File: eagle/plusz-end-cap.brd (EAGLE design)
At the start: 106 x 106 mm, 28 parts, among them U1 TCA9543A-PW, U3 HMC5883L, U4 HMC5883L

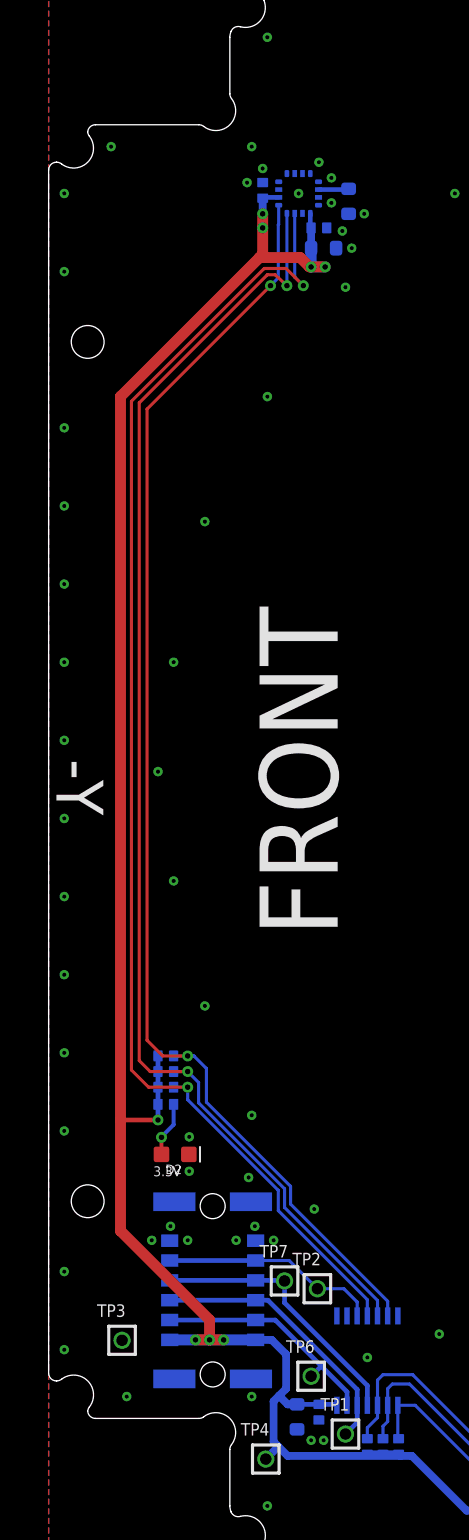
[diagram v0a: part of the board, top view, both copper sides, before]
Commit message: Added cutout for debug connector, update PNG.
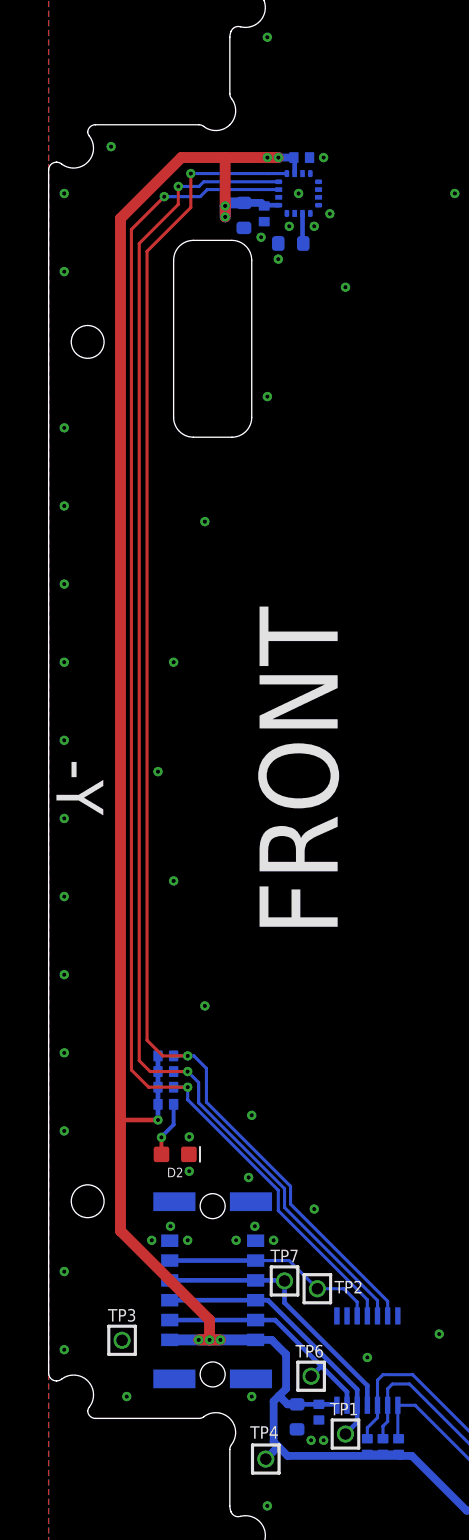
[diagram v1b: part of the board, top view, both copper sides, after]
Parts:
- moved C15 5.52 mm to (12.5, 88.6), turned to 270 degrees
- moved C13 4.58 mm to (15.5, 86.8), turned to 0 degrees
- moved C10 3.61 mm to (13.8, 88.7), turned to 270 degrees
- moved C1 3.26 mm to (16.2, 92.3), turned to 180 degrees
- turned U4 to 270 degrees
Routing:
- net 3.3V: track 218.4 -> 225.7 mm
- net SCL0: track 83.0 -> 88.9 mm
- net SDA0: track 84.8 -> 88.5 mm
- net !INT0: track 87.0 -> 88.6 mm
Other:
- outline, holes or cut-outs redrawn
- board text removed: "3.3V"

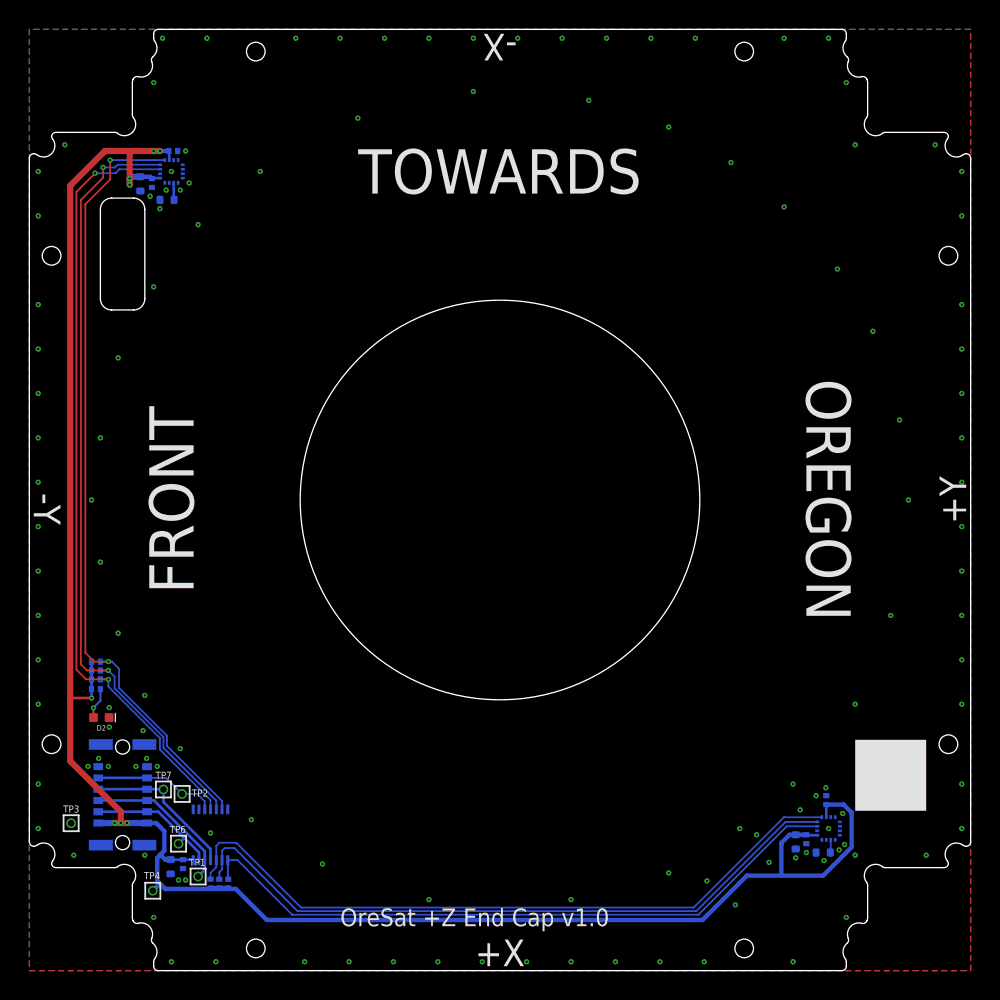
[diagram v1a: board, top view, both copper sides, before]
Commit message: Added updated keepouts for antennas; opened up helical opening.
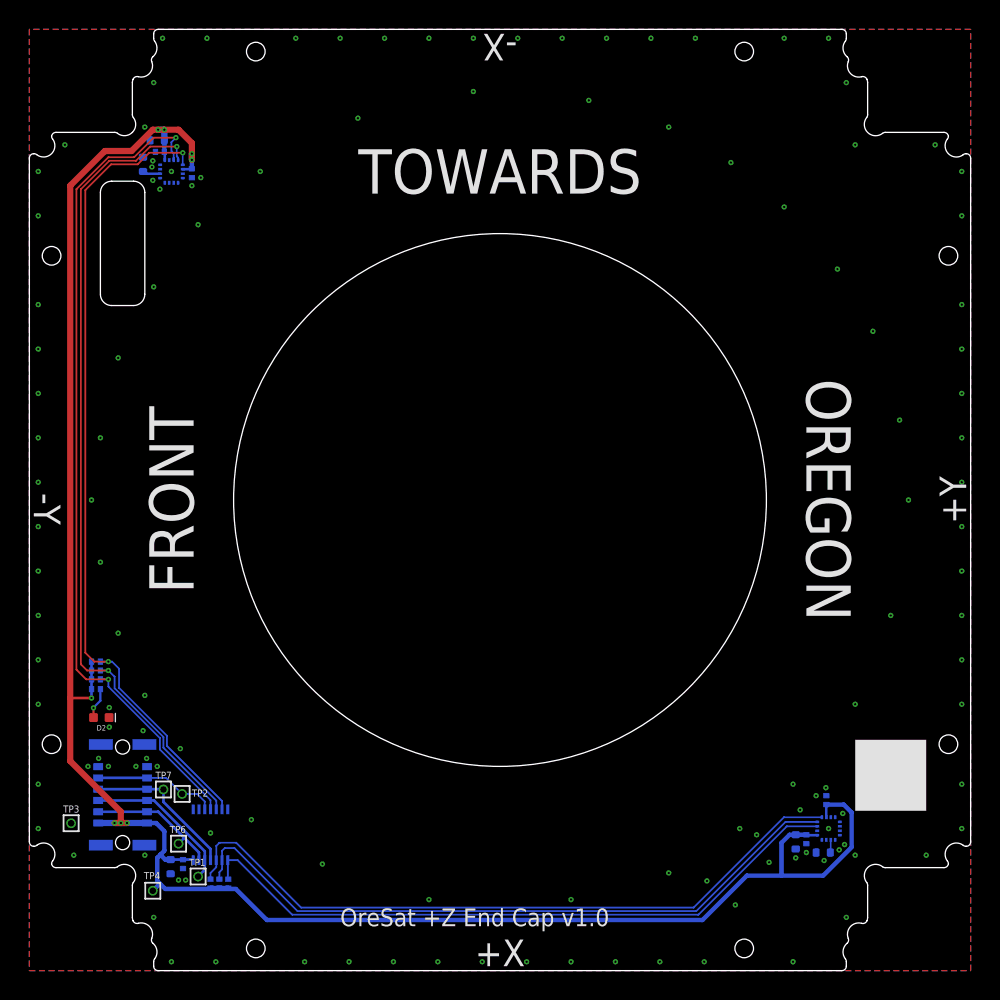
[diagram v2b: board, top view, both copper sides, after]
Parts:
- moved C15 5.26 mm to (14.4, 93.5), turned to 0 degrees
- moved C13 4.83 mm to (12.8, 90.8), turned to 90 degrees
- moved C10 3.61 mm to (14.7, 92.2), turned to 0 degrees
- moved C1 3.26 mm to (18.3, 89.8), turned to 270 degrees
- turned U4 to 0 degrees
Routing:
- net !INT0: track 88.6 -> 94.9 mm
- net SDA0: track 88.5 -> 92.8 mm
- net SCL0: track 88.9 -> 92.3 mm
- net 3.3V: track 225.7 -> 228.8 mm
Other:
- outline, holes or cut-outs redrawn

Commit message: To begin redoing the +Z end cap board, I took the dimension layer from the 9-10-20 version of the board file and replaced it with the new DXF from Hayden Reinhold.
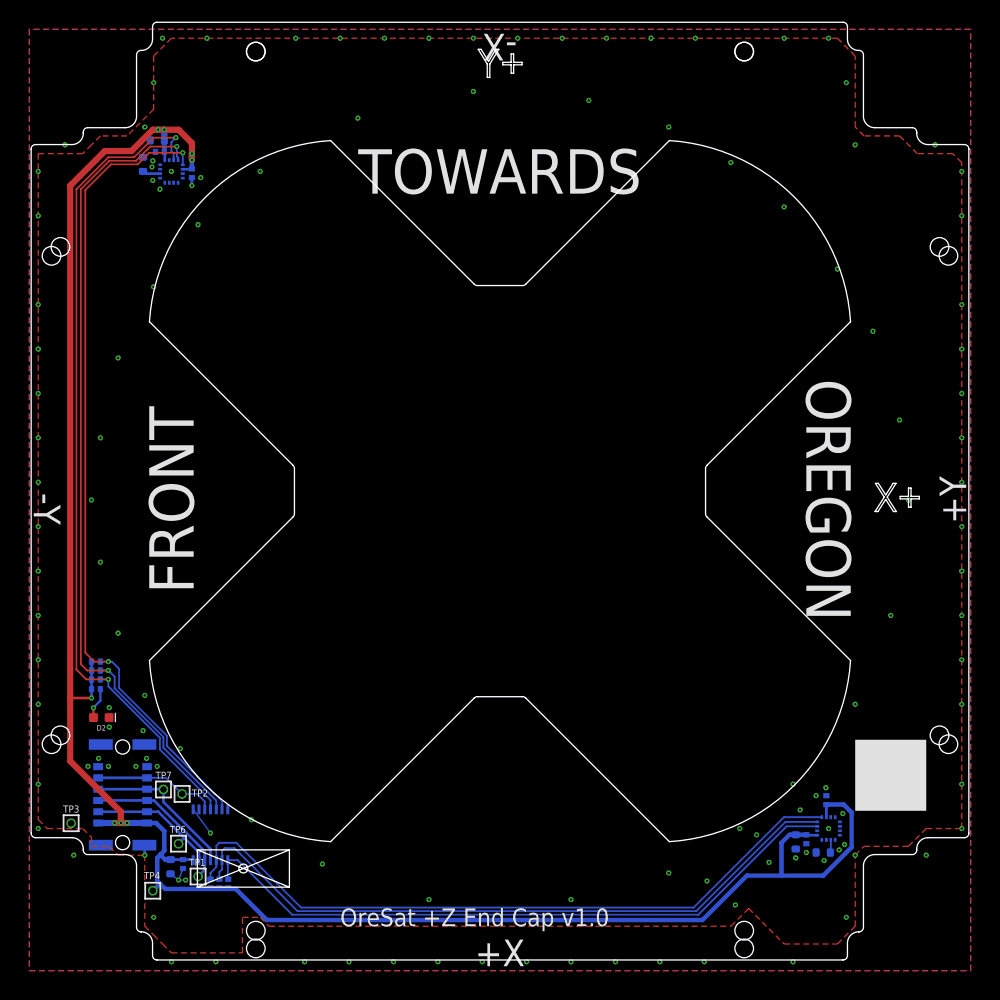
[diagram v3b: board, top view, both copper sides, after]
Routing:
- net GND: track 0.00 -> 8.66 mm
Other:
- board size 106 x 106 mm -> 105.6 x 105.6 mm
